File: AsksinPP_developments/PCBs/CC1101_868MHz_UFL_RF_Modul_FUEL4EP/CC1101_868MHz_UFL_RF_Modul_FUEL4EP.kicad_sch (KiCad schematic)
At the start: 40 parts, among them U1 CC1101RGPR, Y1 Crystal 26MHz

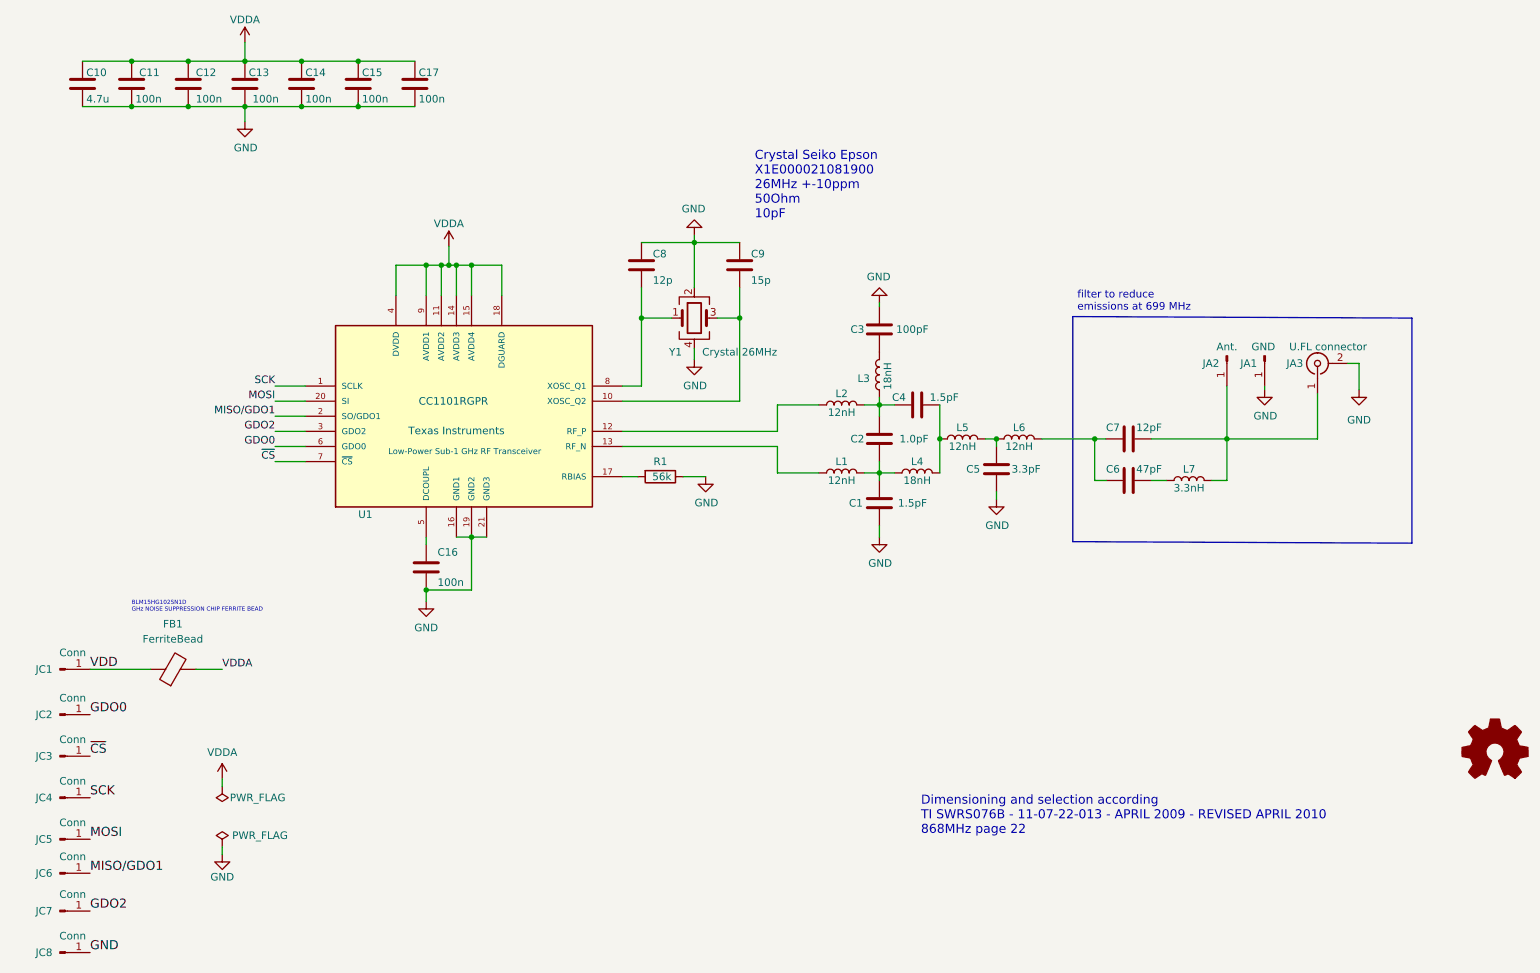
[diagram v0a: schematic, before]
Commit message: PCBs: CC1101_868MHz_UFL_RF_Modul_FUEL4EP: derivated from CC1101_868MHz_RF_Modul_FUEL4EP with improved decoupling capacitor return paths
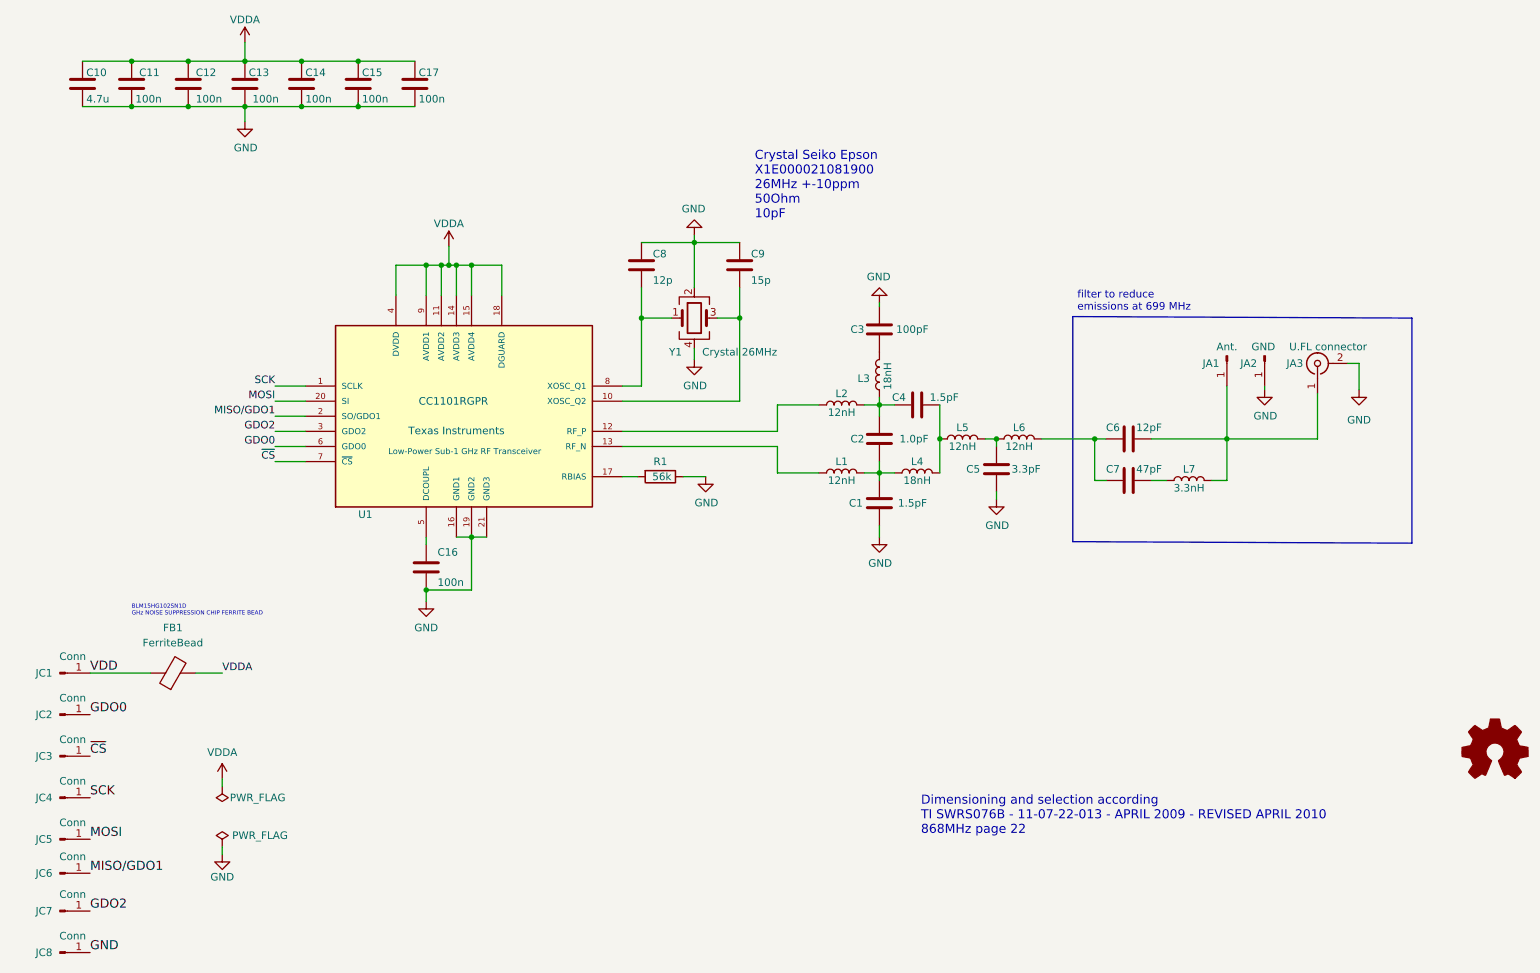
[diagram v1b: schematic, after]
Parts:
- C13: footprint Capacitor_SMD:C_0402_1005Metric -> Capacitor_SMD:C_0603_1608Metric; LCSC C1525 -> C14663; TYPE 0402 -> 0603
- C6: value 47pF -> 12pF; LCSC C384800 -> C1547
- C7: value 12pF -> 47pF; LCSC C1547 -> C384800
- JA1: value GND -> Ant.
- JA2: value Ant. -> GND
- JA3: LCSC (none) -> C598199; TYPE (none) -> SMD
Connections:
- net GND: now also JA2.1 (Pin_1); no longer JA1.1 (Pin_1)
- net at L7.1: now also C7.1; no longer C6.1
- net at JA3.1 (In), L7.2: now also C6.1, JA1.1 (Pin_1); no longer C7.1, JA2.1 (Pin_1)

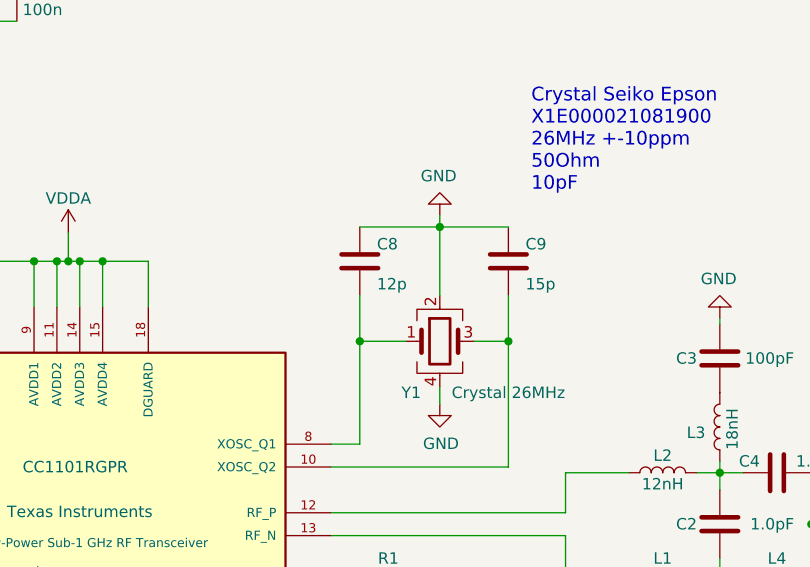
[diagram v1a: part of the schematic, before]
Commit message: PCBs: CC1101_868MHz_RF_Modul_FUEL4EP and CC1101_868MHz_UFL_RF_Modul_FUEL4EP: Reduction of parasitic capaitance of oscillator layout; use 1% CoG capacitors for oscillator
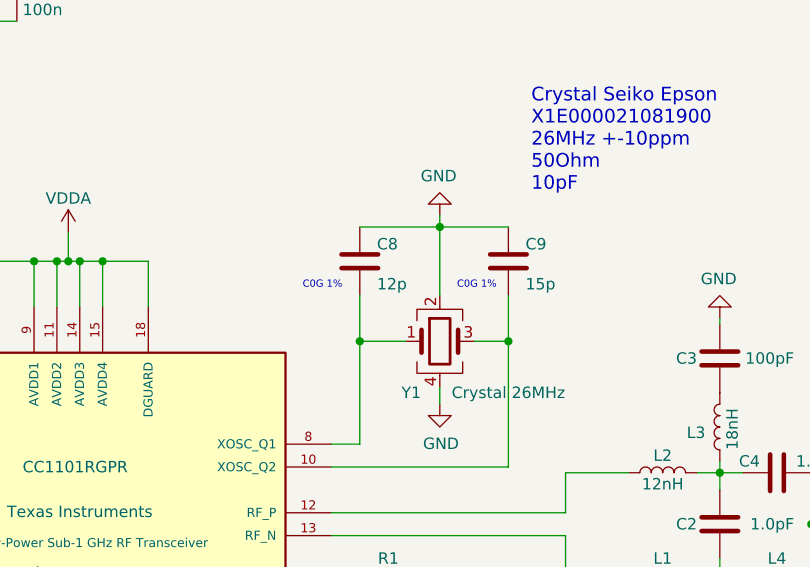
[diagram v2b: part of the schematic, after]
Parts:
- C8: LCSC C1547 -> C393682; Remark (none) -> use C0G ±1% type!
- C9: LCSC C2169087 -> C441742; Remark (none) -> use C0G ±1% type!
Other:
- note added: "C0G 1%"
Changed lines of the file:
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@@
   (title_block
     (title "CC1101_868MHz_UFL_RF_Modul_FUEL4EP")
-    (date "2023-09-21")
-    (rev "1.3")
+    (date "2023-09-29")
+    (rev "1.4")
     (company "(C) FUEL4EP 2023")
     (comment 1 "fork of Jérômes CC1101_module https://github.com/jp112sdl/CC1101_Module ")
@@
     (effects (font (size 0.7 0.7)) (justify left bottom))
   )
+  (text "C0G 1%" (at 123.825 69.215 0)
+    (effects (font (size 0.8 0.8)) (justify left bottom))
+  )
   (text "Dimensioning and selection according \nTI SWRS076B - 11-07-22-013 - APRIL 2009 - REVISED APRIL 2010\n868MHz page 22"
     (at 177.165 161.925 0)
     (effects (font (size 1.524 1.524)) (justify left bottom))
+  )
+  (text "C0G 1%" (at 140.97 69.215 0)
+    (effects (font (size 0.8 0.8)) (justify left bottom))
   )
   (text "filter to reduce\nemissions at 699 MHz" (at 203.454 73.914 0)
@@
       (effects (font (size 1.27 1.27)) hide)
     )
-    (property "LCSC" "C1547" (id 4) (at 130.175 66.04 0)
+    (property "LCSC" "C393682" (id 4) (at 130.175 66.04 0)
       (effects (font (size 1.524 1.524)) hide)
     )
     (property "TYPE" "0402" (id 5) (at 130.175 66.04 0)
+      (effects (font (size 1.524 1.524)) hide)
+    )
+    (property "Remark" "use C0G ±1% type!" (id 6) (at 130.175 66.04 0)
       (effects (font (size 1.524 1.524)) hide)
     )
@@
       (effects (font (size 1.27 1.27)) hide)
     )
-    (property "LCSC" "C2169087" (id 4) (at 146.685 66.04 0)
+    (property "LCSC" "C441742" (id 4) (at 146.685 66.04 0)
       (effects (font (size 1.524 1.524)) hide)
     )
@@
       (effects (font (size 1.524 1.524)) hide)
     )
+    (property "Remark" "use C0G ±1% type!" (id 6) (at 146.685 66.04 0)
+      (effects (font (size 1.524 1.524)) hide)
+    )

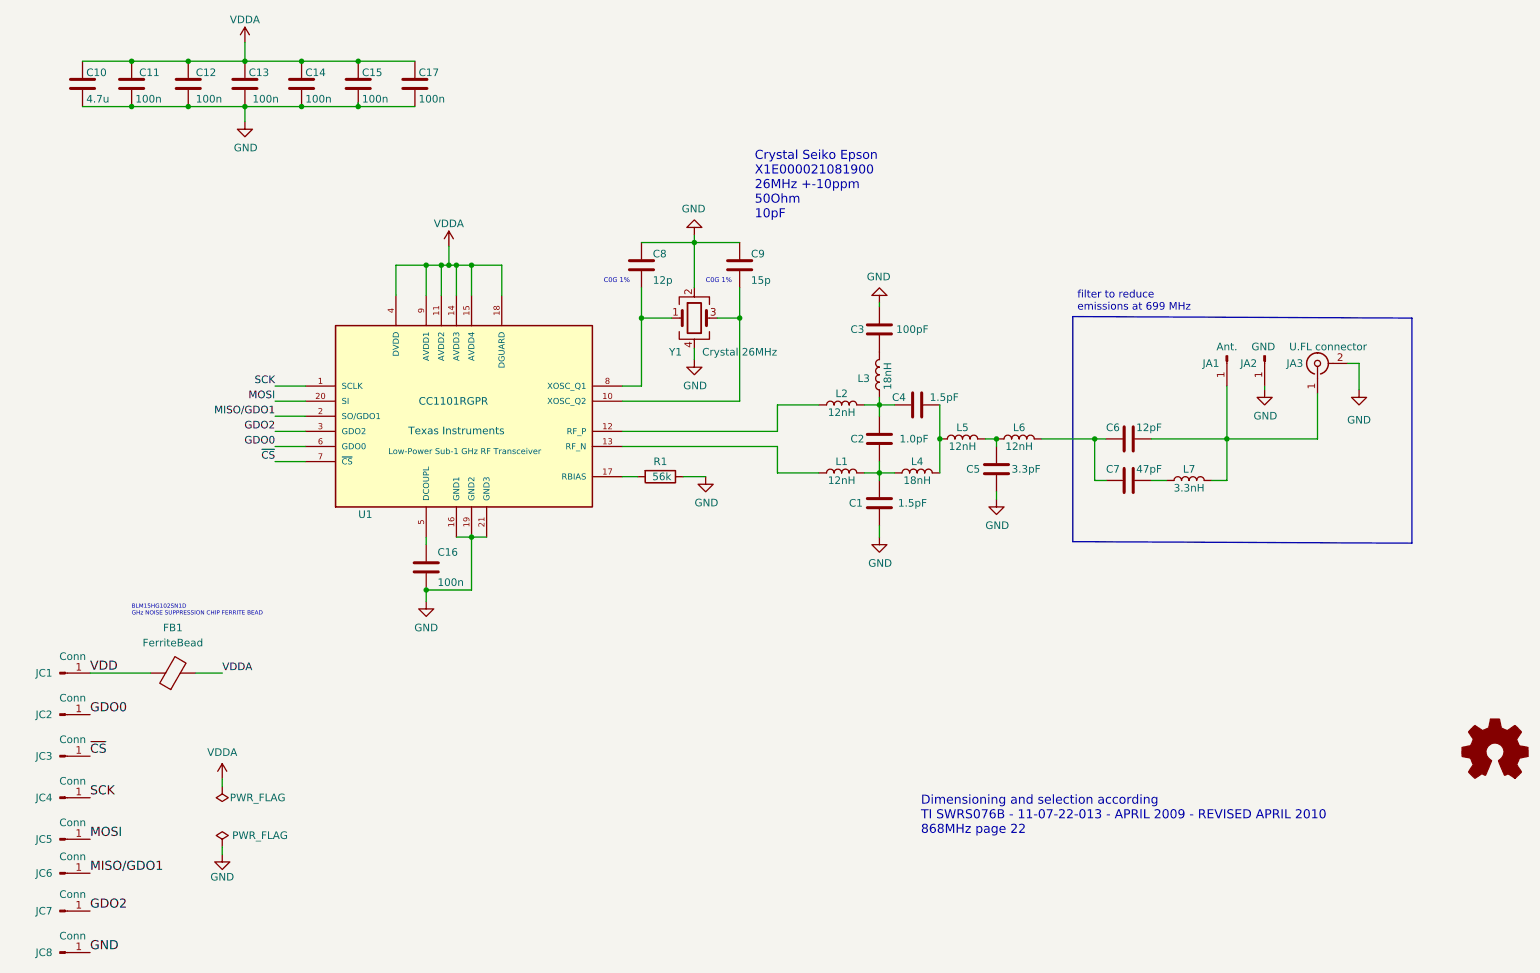
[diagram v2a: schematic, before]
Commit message: PCBs/CC1101_868MHz_UFL_RF_Modul_FUEL4EP: migration to KiCAD 8
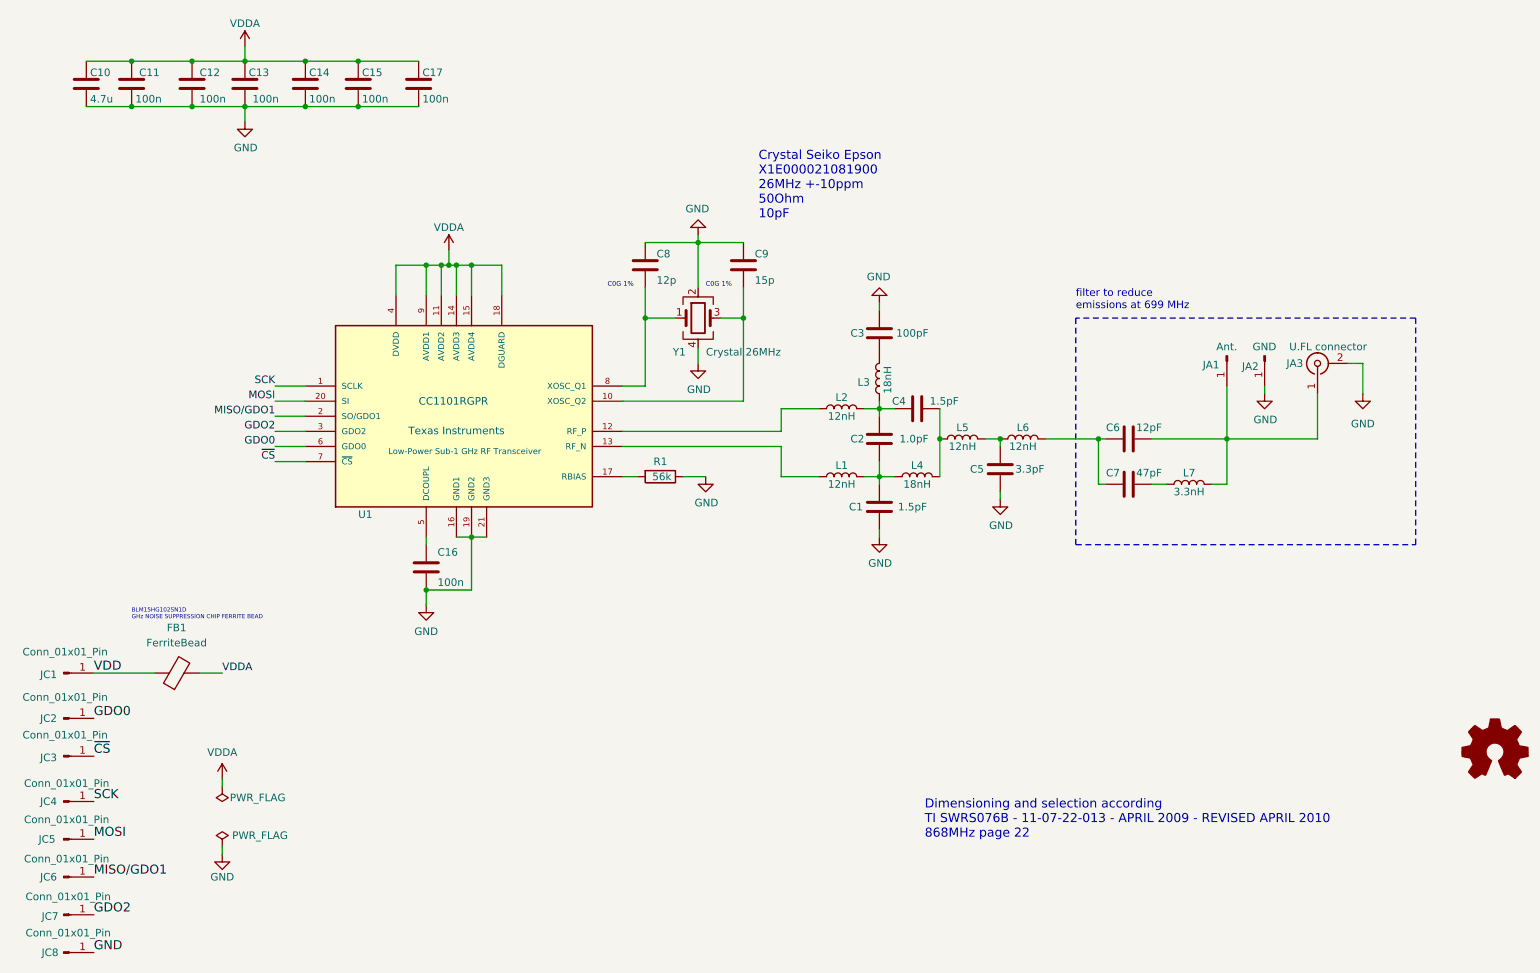
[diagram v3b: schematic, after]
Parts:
- removed JA1: Ant., FUEL4EP:edge_hole_Pitch2.28mm_Drill0.8mm, symbol Connector:Conn_01x01_Male
- removed JA2: GND, FUEL4EP:edge_hole_Pitch2.28mm_Drill0.8mm, symbol Connector:Conn_01x01_Male
- removed JC1: Conn, FUEL4EP:edge_hole_Pitch1.27mm_Drill0.75mm, symbol Connector:Conn_01x01_Male
- removed JC2, JC3, JC4, JC5, JC6, JC7, JC8: Conn, FUEL4EP:edge_hole_Pitch1.27mm_Drill0.75mm_rounded, symbol Connector:Conn_01x01_Male
- added JA1: Ant., FUEL4EP:edge_hole_Pitch1.27mm_Drill0.75mm, symbol Connector:Conn_01x01_Pin
- added JA2: GND, FUEL4EP:edge_hole_Pitch1.27mm_Drill0.75mm, symbol Connector:Conn_01x01_Pin
- added JC1: Conn_01x01_Pin, FUEL4EP:edge_hole_Pitch1.27mm_Drill0.75mm, symbol Connector:Conn_01x01_Pin
- added JC2, JC3, JC4, JC5, JC6, JC7, JC8: Conn_01x01_Pin, FUEL4EP:edge_hole_Pitch1.27mm_Drill0.75mm_rounded, symbol Connector:Conn_01x01_Pin
- U1: footprint Package_DFN_QFN:Texas_S-PVQFN-N20_EP2.4x2.4mm_ThermalVias -> Package_DFN_QFN:Texas_RGP0020H_VQFN-20-1EP_4x4mm_P0.5mm_EP2.4x2.4mm_ThermalVias; Description_1 (none) -> Low-Power Sub-1 GHz RF Transceiver
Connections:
- net GDO0: now also JC2.1 (Pin_1)
- net GDO2: now also JC7.1 (Pin_1)
- net GND: now also JA2.1 (Pin_1), JC8.1 (Pin_1)
- net MISO/GDO1: now also JC6.1 (Pin_1)
- net MOSI: now also JC5.1 (Pin_1)
- net SCK: now also JC4.1 (Pin_1)
- net VDD: now also JC1.1 (Pin_1)
- net ~{CS}: now also JC3.1 (Pin_1)
- net at C6.1, JA3.1 (In), L7.2: now also JA1.1 (Pin_1)
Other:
- moved on the sheet: C1, C10, C12, C14, C17, C3, C4, C5, C7, C8, C9, FB1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
